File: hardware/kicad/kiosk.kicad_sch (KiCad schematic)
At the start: 16 parts, among them J10 Jack 5V rail 1, J11 Jack 5V rail 2, J12 Spare PCF8574, J3 LCD 4.0in ST7796S + GT911, J4 VL53L1X, J5 PCF8574 0x20, J6 DS3231, J7 MAX98357A, J8 Speaker 4ohm 3W, J9 SG90 servo, U1 ESP32-S3-CAM N16R8

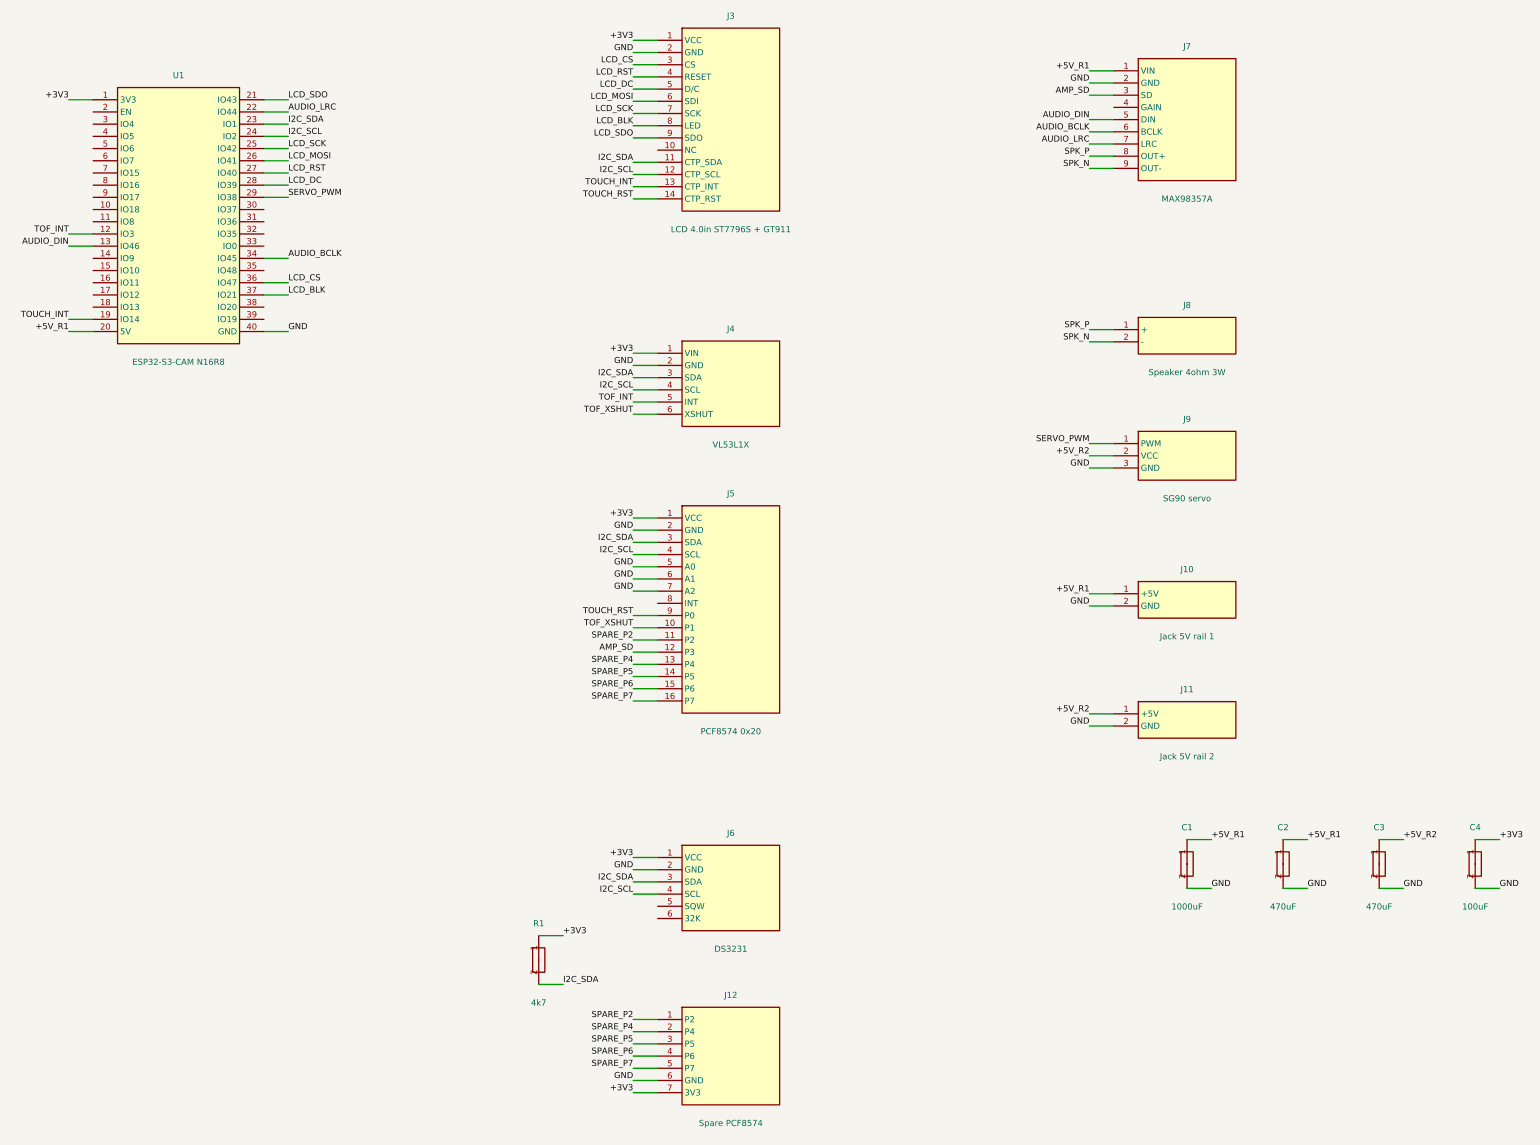
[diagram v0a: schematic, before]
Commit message: feat(hardware): clear the schematic through ERC and export the report figure
kicad-cli turned out to be installed at /mnt/d/KiCad and runs from WSL, so
the schematic could finally be checked by KiCad itself rather than by my
own reading of it. It had 150 violations.

106 were off-grid endpoints. Symbols sat at round millimetre positions -
75, 190, 285 - and none of those is a multiple of the 1.27 mm connection
grid, so every pin was off it and wires drawn later in the GUI would have
refused to attach. Placement now snaps to 2.54 mm, which puts each pin on
the grid whatever the pin count.

27 were pins left open on purpose: the camera lines on the devkit, EN, the
panel's NC, GAIN, SQW and 32K. They carry no-connect flags now, which is
how that intent is stated rather than implied.

It also caught a name I had guessed wrong. The three screw terminals
pointed at TerminalBlock_bornier-2_P5.08mm, which does not exist; every
footprint is now checked against the installed libraries and all sixteen
resolve.

The 17 left all say the kiosk library is not in the configuration, and
they survive KIPRJMOD being set by hand, so kicad-cli does not read
project library tables. The symbols are extracted into a real library and
both tables are committed; confirm the count in the GUI.

Task: E14-T8
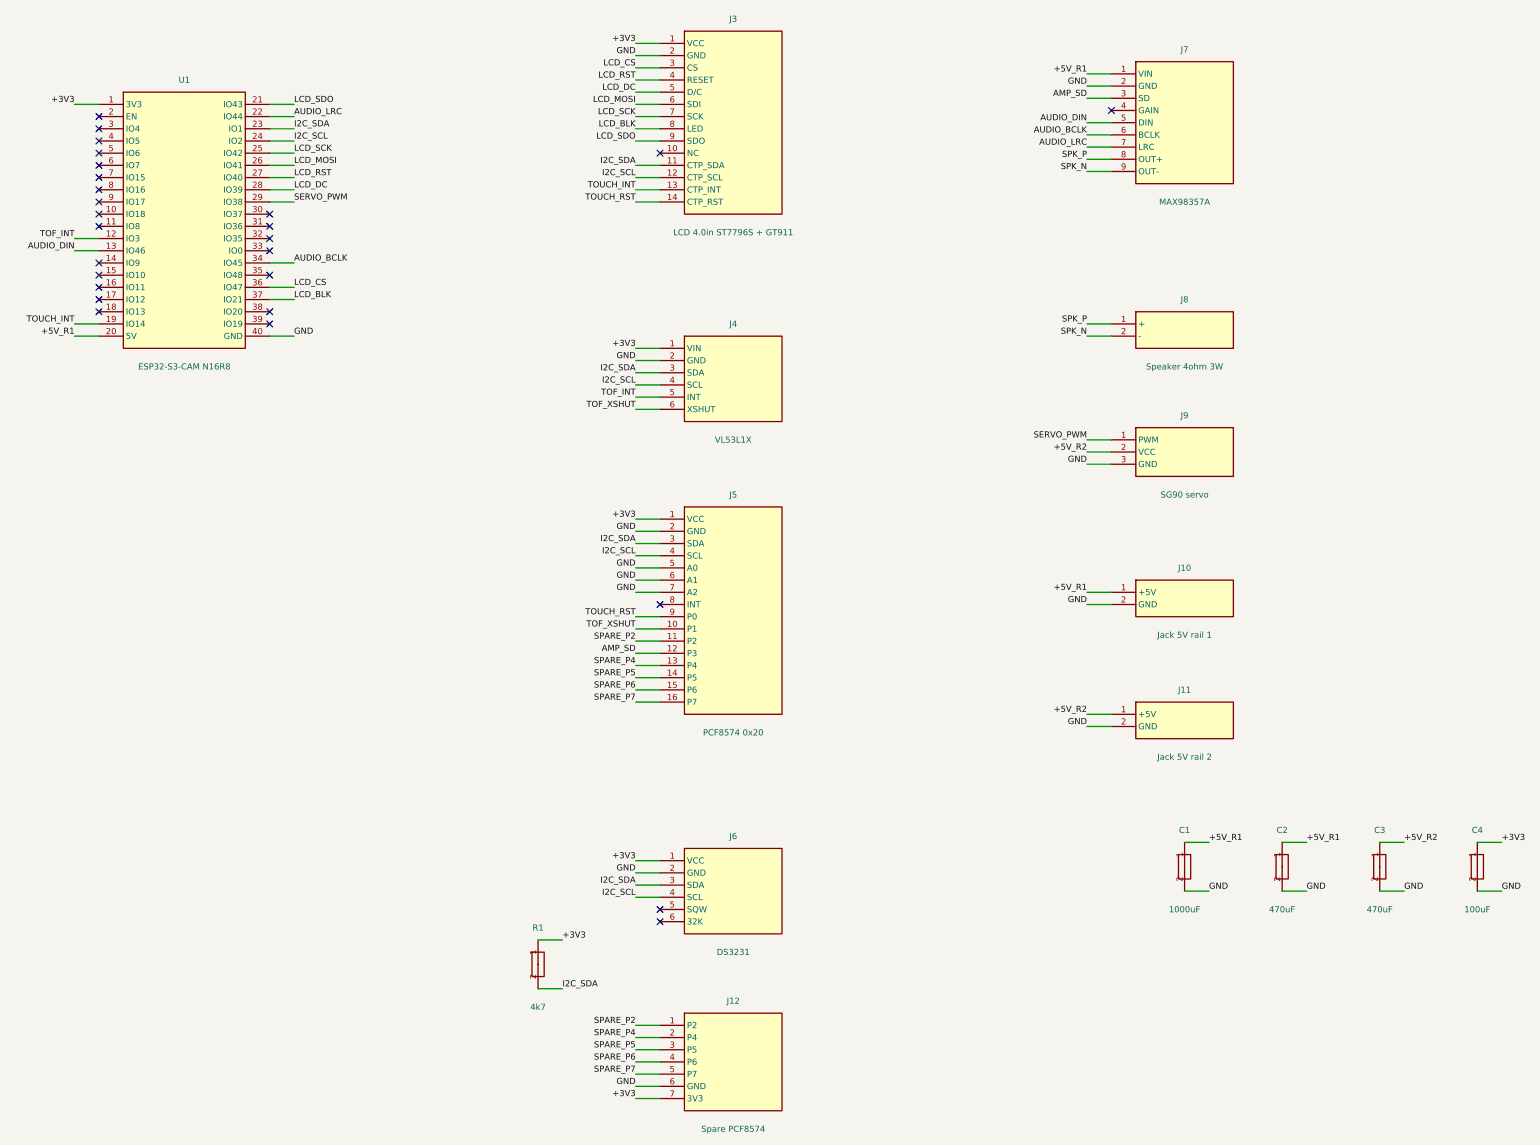
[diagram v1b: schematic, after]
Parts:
- J10, J11, J8: footprint TerminalBlock:TerminalBlock_bornier-2_P5.08mm -> TerminalBlock:TerminalBlock_MaiXu_MX126-5.0-02P_1x02_P5.00mm
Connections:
- no-connect marks 0 -> 27
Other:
- moved on the sheet: C1, C2, C3, C4, J10, J11, J12, J3, J4, J5, J6, J7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

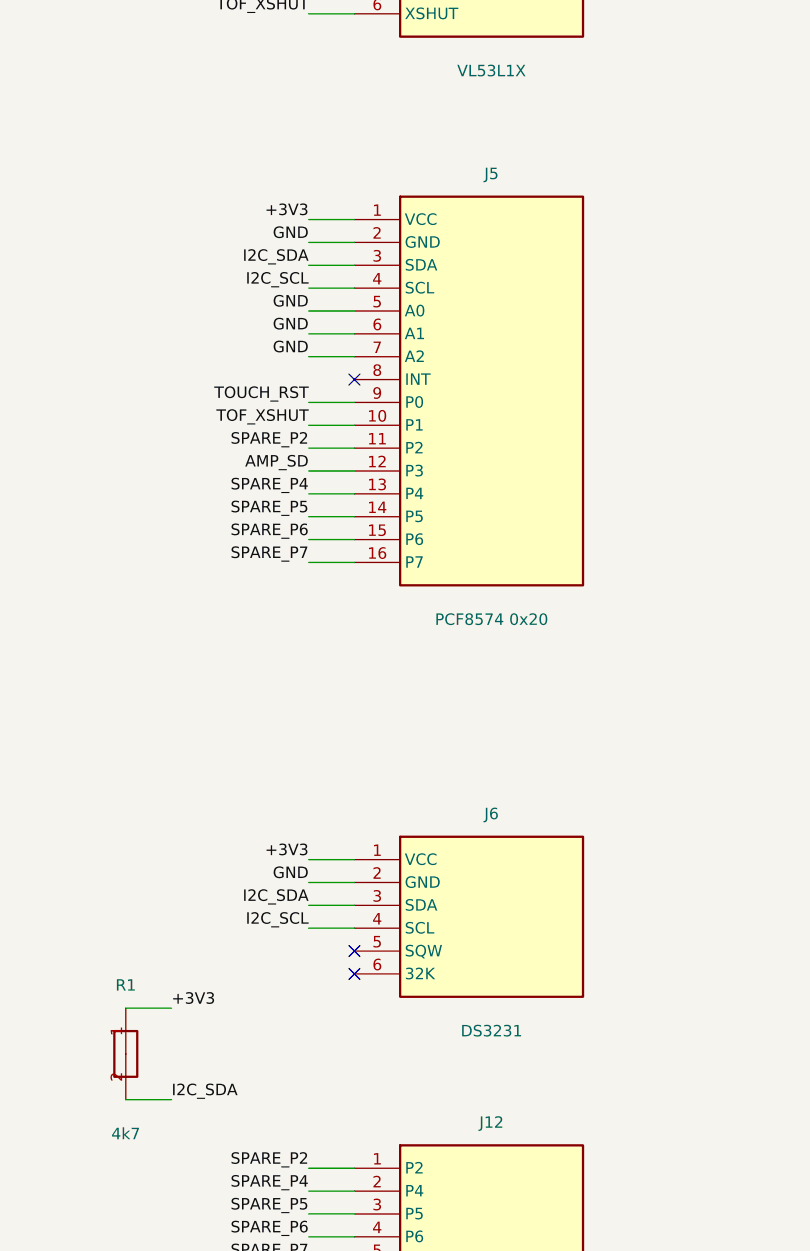
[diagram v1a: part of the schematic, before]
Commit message: fix(hardware): the expander has two rows, not one, and no address pins
J5 was drawn as a single row of sixteen carrying VCC, GND, SDA, SCL,
A0..A2 and P0..P7. The module in hand has nothing like it: four pins on
its bottom edge for the bus, nine down its right edge for the port, the
two perpendicular, and A0/A1/A2 are solder pads on the module rather than
pins. I guessed a pinout instead of looking at the part - the same
mistake as the terminal block footprint, but this one landed in the
netlist rather than in a name.

So J5 becomes the four-pin bus row and J13 the nine-pin port row, and the
three address lines leave the schematic: no copper on the carrier reaches
them, and section 2.3G now says they are jumpered to GND on the module
itself. Eighty-seven connection points where there were ninety.

Placement is redone around what the kiosk has to face: the panel hangs off
the top edge on the same plane as the board, the camera looks out of the
devkit below it, and the ToF sits between the two. The rest is sorted by
current - the bus above y=31, everything that switches below y=55, 24 mm
between them.

Still owed: the expander's two rows are placed where they look tidy, not
where its own geometry puts them, so that spacing is marked for
measurement. The three other modules carry pinouts I read the same way I
read this one, and none has been checked against the part.
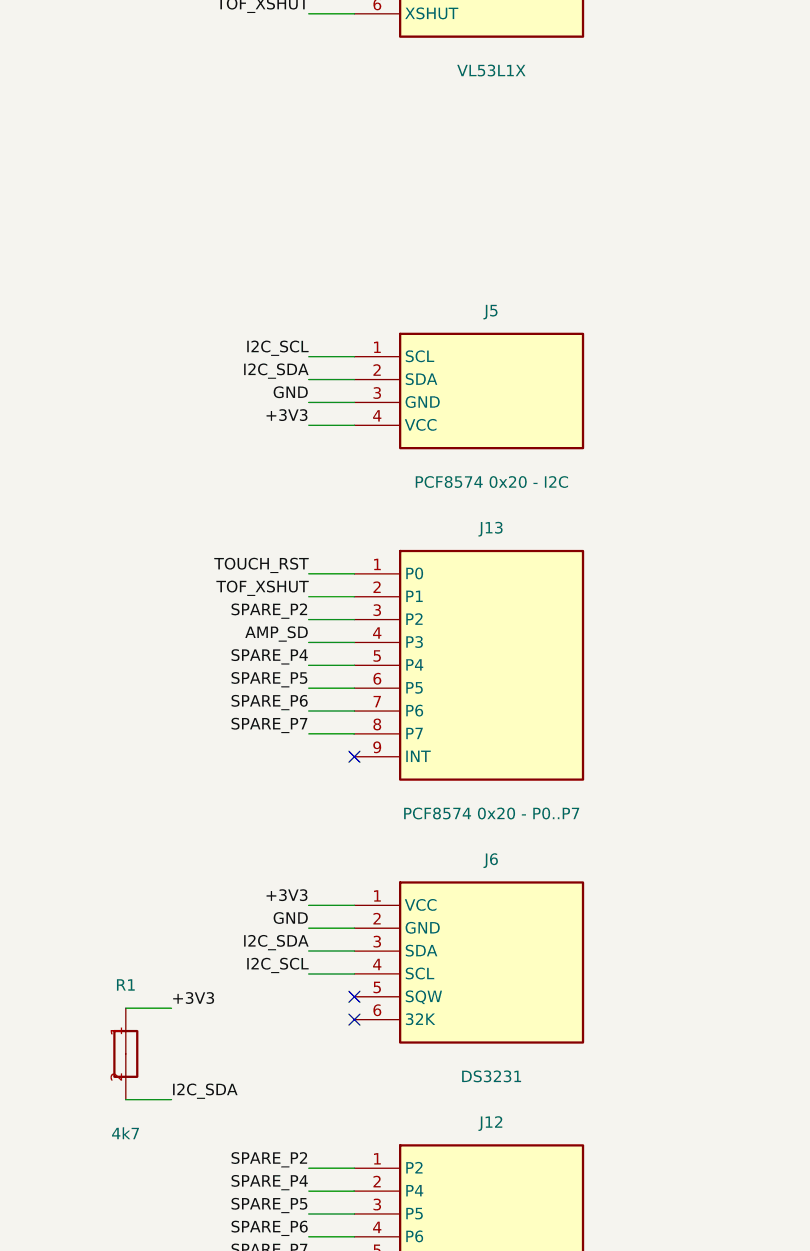
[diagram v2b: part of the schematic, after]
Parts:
- added J13: PCF8574 0x20 - P0..P7, Connector_PinSocket_2.54mm:PinSocket_1x09_P2.54mm_Vertical, symbol kiosk:J13
- J5: value PCF8574 0x20 -> PCF8574 0x20 - I2C; footprint Connector_PinSocket_2.54mm:PinSocket_1x16_P2.54mm_Vertical -> Connector_PinSocket_2.54mm:PinSocket_1x04_P2.54mm_Vertical
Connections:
- net +3V3: now also J5.4 (VCC); no longer J5.1 (VCC)
- net AMP_SD: now also J13.4 (P3); no longer J5.12 (P3)
- net GND: now also J5.3 (GND); no longer J5.2 (GND), J5.5 (A0), J5.6 (A1), J5.7 (A2)
- net I2C_SCL: now also J5.1 (SCL); no longer J5.4 (SCL)
- net I2C_SDA: now also J5.2 (SDA); no longer J5.3 (SDA)
- net SPARE_P2: now also J13.3 (P2); no longer J5.11 (P2)
- net SPARE_P4: now also J13.5 (P4); no longer J5.13 (P4)
- net SPARE_P5: now also J13.6 (P5); no longer J5.14 (P5)
- net SPARE_P6: now also J13.7 (P6); no longer J5.15 (P6)
- net SPARE_P7: now also J13.8 (P7); no longer J5.16 (P7)
- net TOF_XSHUT: now also J13.2 (P1); no longer J5.10 (P1)
- net TOUCH_RST: now also J13.1 (P0); no longer J5.9 (P0)
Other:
- moved on the sheet: J6
